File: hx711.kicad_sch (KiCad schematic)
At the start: 16 parts, among them Q1 S8550, U6 HX711

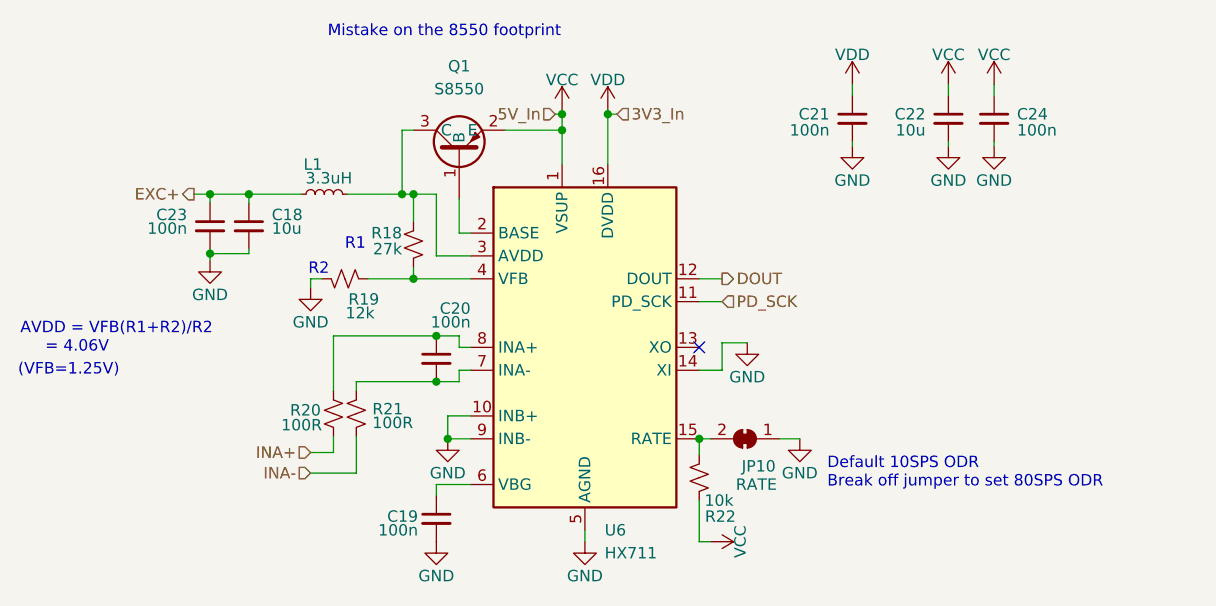
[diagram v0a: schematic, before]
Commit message: Update BJT symbols and ver number
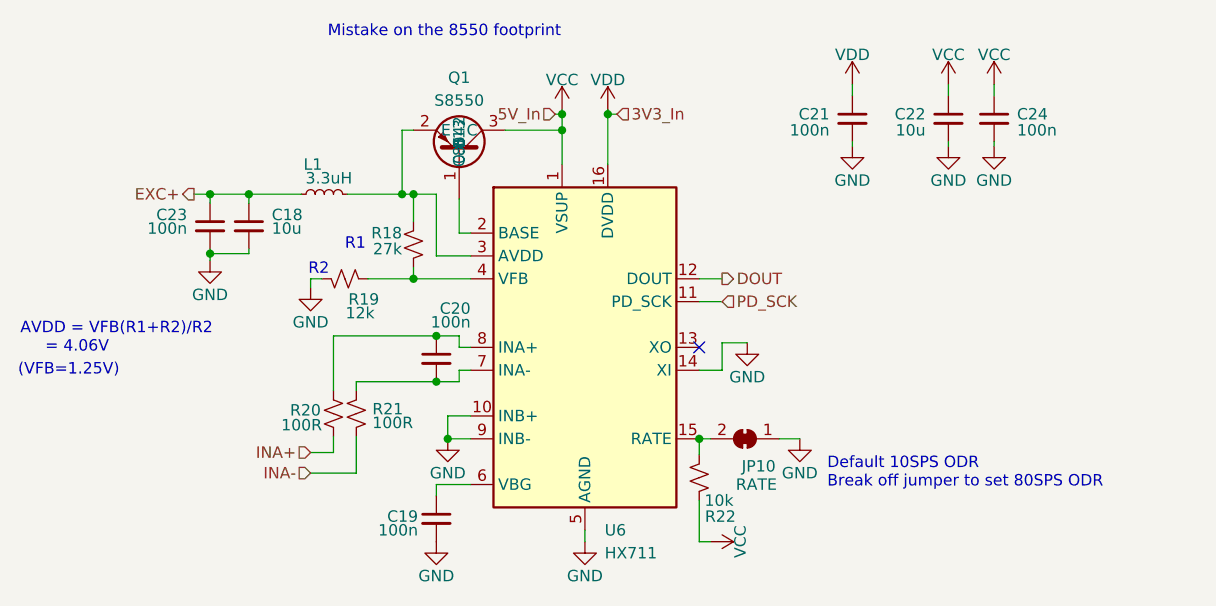
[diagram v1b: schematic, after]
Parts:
- Q1: symbol sensify:8550 -> UCT:S8550_SMD; Extended (none) -> 0; LCSC (none) -> C8542; Price (none) -> 0.013
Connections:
- net VCC: now also Q1.3 (C); no longer Q1.2 (E)
- net at L1.2, R18.1, U6.3 (AVDD): now also Q1.2 (E); no longer Q1.3 (C)
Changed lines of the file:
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@@
     (title "HX711 Circuit")
     (date "2023-12-05")
-    (rev "1.1.0")
+    (rev "1.2.0")
     (company "https://learn.sparkfun.com/tutorials/load-cell-amplifier-hx711-breakout-hookup-guide")
   )
@@
     )
   )
-  (symbol (lib_id "sensify:8550") (at 130.81 67.31 270) (mirror x) (unit 1)
-    (in_bom yes) (on_board yes) (dnp no)
-    (property "Reference" "Q1" (at 130.81 60.198 90)
-      (effects (font (size 1.27 1.27)))
-    )
-    (property "Value" "S8550" (at 130.81 62.738 90)
-      (effects (font (size 1.27 1.27)))
-    )
-    (property "Footprint" "Package_TO_SOT_SMD:SOT-23" (at 130.81 49.53 0)
-      (effects (font (size 1.27 1.27)) hide)
-    )
-    (property "Datasheet" "https://datasheet.lcsc.com/lcsc/2304140030_Jiangsu-Changjing-Electronics-Technology-Co---Ltd--S8550_C105432.pdf" (at 116.84 68.58 0)
-      (effects (font (size 1.27 1.27)) hide)
-    )
-    (pin "1")
+  (symbol (lib_id "UCT:S8550_SMD") (at 130.81 68.58 270) (mirror x) (unit 1)
+    (in_bom yes) (on_board yes) (dnp no)
+    (property "Reference" "Q1" (at 130.81 61.468 90)
+      (effects (font (size 1.27 1.27)))
+    )
+    (property "Value" "S8550" (at 130.81 64.008 90)
+      (effects (font (size 1.27 1.27)))
+    )
+    (property "Footprint" "Package_TO_SOT_SMD:SOT-23" (at 130.81 68.58 0)
+      (effects (font (size 1.27 1.27)) hide)
+    )
+    (property "Datasheet" "https://datasheet.lcsc.com/lcsc/1810161212_Jiangsu-Changjing-Electronics-Technology-Co---Ltd--SS8550-Y2_C8542.pdf" (at 130.81 68.58 0)
+      (effects (font (size 1.27 1.27)) hide)
+    )
+    (property "LCSC" "C8542" (at 130.81 68.58 0)
+      (effects (font (size 1.27 1.27)))
+    )
+    (property "Extended" "0" (at 130.81 68.58 0)
+      (effects (font (size 1.27 1.27)))
+    )
+    (property "Price" "0.013" (at 130.81 68.58 0)
+      (effects (font (size 1.27 1.27)))
+    )
+    (pin "1")

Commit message: Connected NO2 to COM1. Annonated relays.
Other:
- title: HX711 Circuit -> Raspberry Pi Zero Intrumentation HAT
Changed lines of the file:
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@@
   (paper "A4")
   (title_block
-    (title "HX711 Circuit")
-    (date "2023-12-05")
-    (rev "1.2.0")
+    (title "Raspberry Pi Zero Intrumentation HAT")
+    (date "2024-06-07")
+    (rev "1.3.0")
     (company "https://learn.sparkfun.com/tutorials/load-cell-amplifier-hx711-breakout-hookup-guide")
+    (comment 1 "@supervisor Justin Pead")
+    (comment 2 "@author Montso Mokake")
   )
   (junction (at 147.32 65.532) (diameter 0) (color 0 0 0 0)

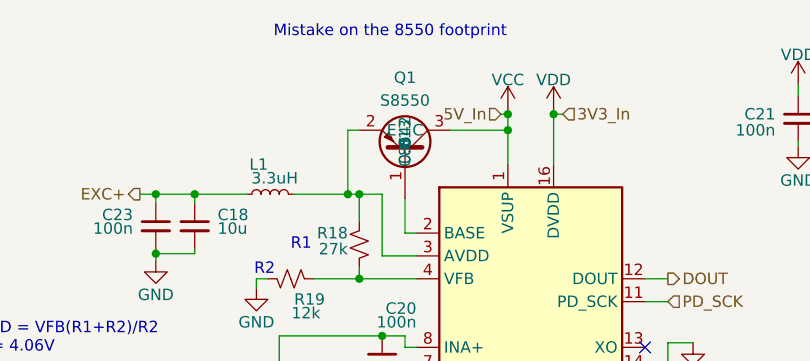
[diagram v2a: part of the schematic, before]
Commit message: Ammended it to have the jumper connection
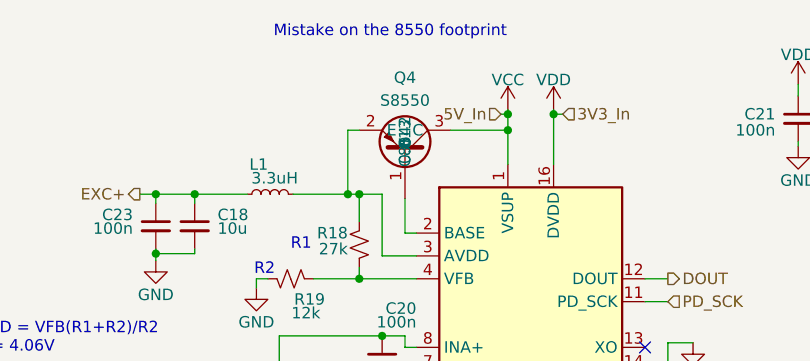
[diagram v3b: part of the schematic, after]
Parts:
- renumbered Q1 to Q4
